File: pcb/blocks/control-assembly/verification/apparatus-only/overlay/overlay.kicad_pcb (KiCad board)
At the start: 6 copper layers, 164 x 234 mm, 168 parts, among them J1 ?, J2 ?, K1 ?, K2 ?, K3 ?, Q1 ?, Q2 ?, SW1 ?, SW2 ?, T1 ?, T2 ?, U1 ?, U10 ?, U11 ?, U12 ?, U13 ?, U14 ?, U15 ?, U16 ?, U17 ?, U18 ?, U19 ?, U2 ?, U20 ?, U21 ?, U22 ?, U23 ?, U24 ?, U25 ?, U26 ?, U27 ?, U3 ?, U4 ?, U5 ?, U6 ?, U7 ?, U8 ?, U9 ?

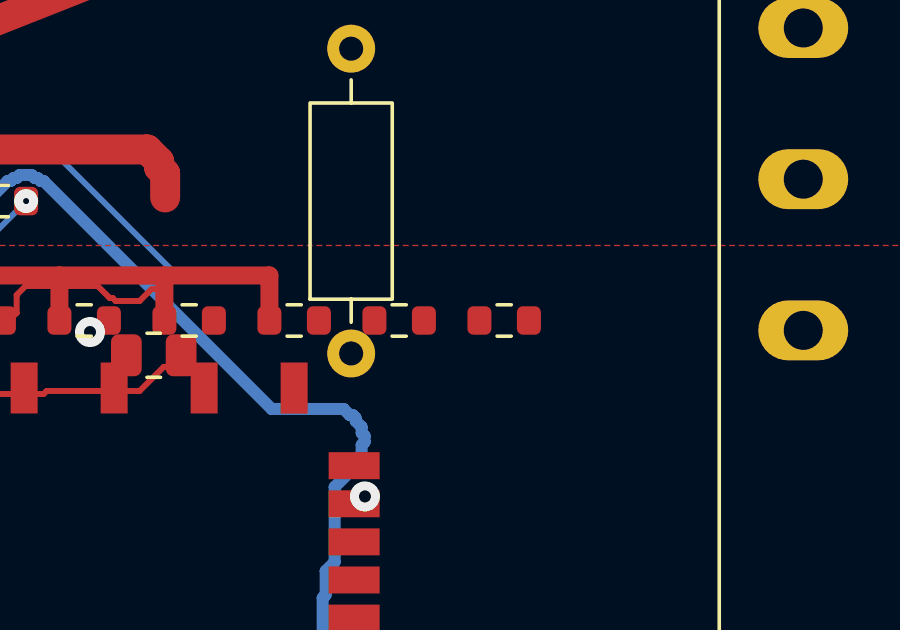
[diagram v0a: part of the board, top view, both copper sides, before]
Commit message: fix(control-assembly): flat schematic parity, prototype vendor fallback, overlay net re-assert
- compose_assembly: use the flat strict-candidate schematic layout and pass
  BOM values into generate_candidate_board, moving schematic parity 98 -> 0
  (19 footprint_symbol_mismatch + 79 net_conflict). Regenerate the combined
  bridge/source map so SW1/SW2 are the real SW_SPST_EVQP7A.
- block_source: fall back to the buck prototype library for footprints absent
  from KiCad stock and pcb/libs, recording prototype-lib provenance; drop
  compose_assembly._stock_root_with_overrides. Persist
  assembly-candidate/library-provenance.json.
- run_block.build_assembly_task_contract: derive the pad census from pad
  identities, not physical pad count (a real switch repeats 1,1,2,2); mirrors
  the accepted MCU-profile fix.
- run_control_assembly: re-assert production track net identity by name after
  the KiCad refill so net_reassigned is 0; measure ground continuity across
  the section/production boundary. The section-pour clip was implemented and
  measured to raise introduced findings and break the cross-view endpoints, so
  it is recorded as rejected (enabled false), not silently omitted.
- compose_blocks: compare zone identity (net/layer/filled), not polygon
  subdivision, in the cross-view comparison.
- tests + docs updated for the above.
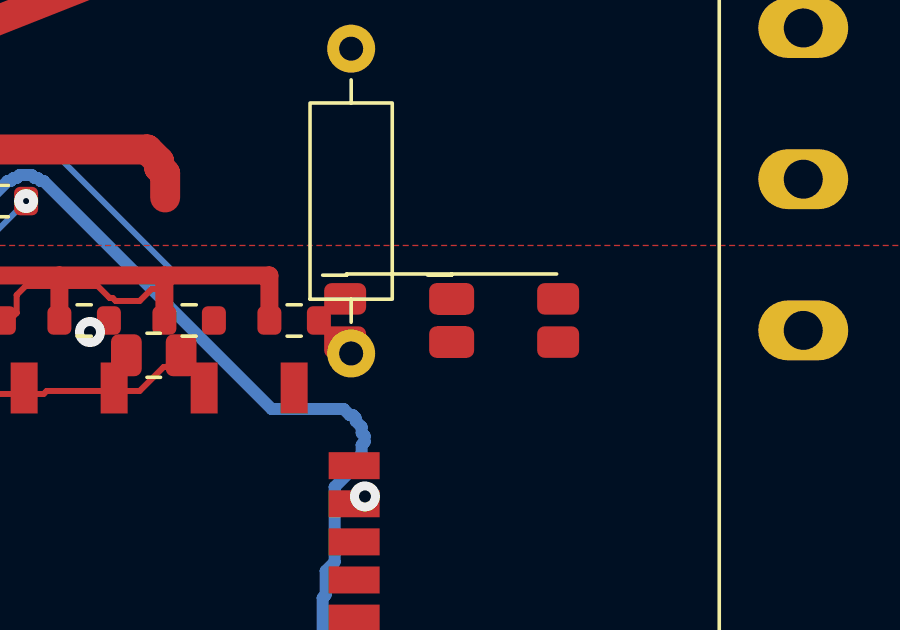
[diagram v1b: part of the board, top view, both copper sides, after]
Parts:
- C10, C13, C39: value ? -> C0603C104K5RACTU
- C11, C12: value ? -> CL32B226KAJNNWE
- C40: value ? -> GRM21BR71A106KE51L
- C41: value ? -> GRM188R71A105KA61D
- C9: value ? -> CL32B106KBJZW6E
- L2: value ? -> SRP1265A-5R6M
- R16: value ? -> RC0603FR-07100KL
- R17: value ? -> RC0603FR-0722K1L
- R71, R72: value ? -> RC0603FR-0710KL
- R73, R74: value ? -> RC0603FR-074K7L
- SW1, SW2: value ? -> EVQ-P7A01P; footprint Resistor_SMD:R_0603_1608Metric -> Button_Switch_SMD:SW_SPST_EVQP7A
- U27: value ? -> ESP32-S3-WROOM-1-N8R8
- U3: value ? -> LMR51430XDDCR
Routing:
- net +3V3: vias 26 -> 31
- net io0: vias 1 -> 0
- net gpio21: vias 1 -> 0
- net gnd: vias 67 -> 60
- net V_BUS_SENSE: vias 1 -> 3
- net +15V: vias 6 -> 8
